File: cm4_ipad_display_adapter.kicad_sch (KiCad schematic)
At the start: 2 parts, among them J4 Conn_01x02_Female, U2 MIC5504-1.8YM5

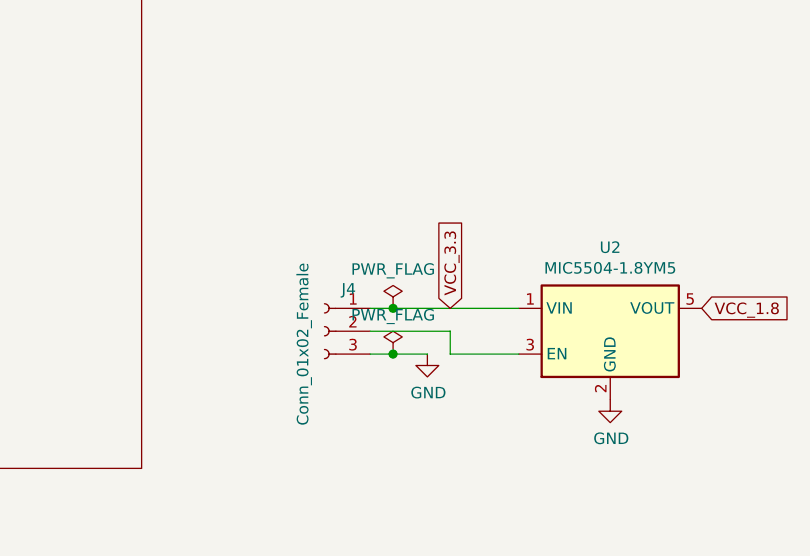
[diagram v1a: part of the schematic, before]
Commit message: Fix ERC errors
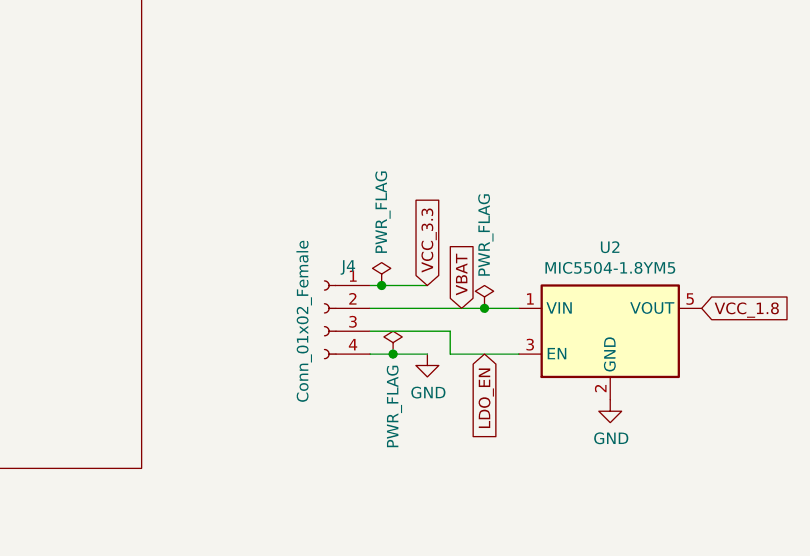
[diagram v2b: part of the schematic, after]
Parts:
- J4: symbol Connector:Conn_01x03_Female -> Connector:Conn_01x04_Female
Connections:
- net GND: now also J4.4 (Pin_4); no longer J4.3 (Pin_3)
- net VCC_3.3: no longer U2.1 (VIN)
- net LDO_EN: now reaches U2.3 (EN)
- net LDO_EN: now also J4.3 (Pin_3); no longer J4.2 (Pin_2)
- new net VBAT: J4.2 (Pin_2), U2.1 (VIN)

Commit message: Add footprints for LED driver HEAD associated components, route them. Fix DRC issues, and add an edge cut.
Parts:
- J4: footprint Connector_PinHeader_2.54mm:PinHeader_1x03_P2.54mm_Vertical -> Connector_PinHeader_2.54mm:PinHeader_1x04_P2.54mm_Vertical
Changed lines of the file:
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@@
     (property "Reference" "J4" (id 0) (at 128.422 85.503 0))
     (property "Value" "Conn_01x02_Female" (id 1) (at 123.3424 91.6113 90))
-    (property "Footprint" "Connector_PinHeader_2.54mm:PinHeader_1x03_P2.54mm_Vertical" (id 2) (at 125.73 90.17 0)
+    (property "Footprint" "Connector_PinHeader_2.54mm:PinHeader_1x04_P2.54mm_Vertical" (id 2) (at 125.73 90.17 0)
       (effects (font (size 1.27 1.27)) hide)
     )
@@
     )
     (path "/a946a672-0361-4eb9-a0a1-9c0b5f6de790"
-      (reference "J4") (unit 1) (value "Conn_01x02_Female") (footprint "Connector_PinHeader_2.54mm:PinHeader_1x03_P2.54mm_Vertical")
+      (reference "J4") (unit 1) (value "Conn_01x02_Female") (footprint "Connector_PinHeader_2.54mm:PinHeader_1x04_P2.54mm_Vertical")
     )
     (path "/7cf1659e-8585-4172-8c4c-c99ac927965b"

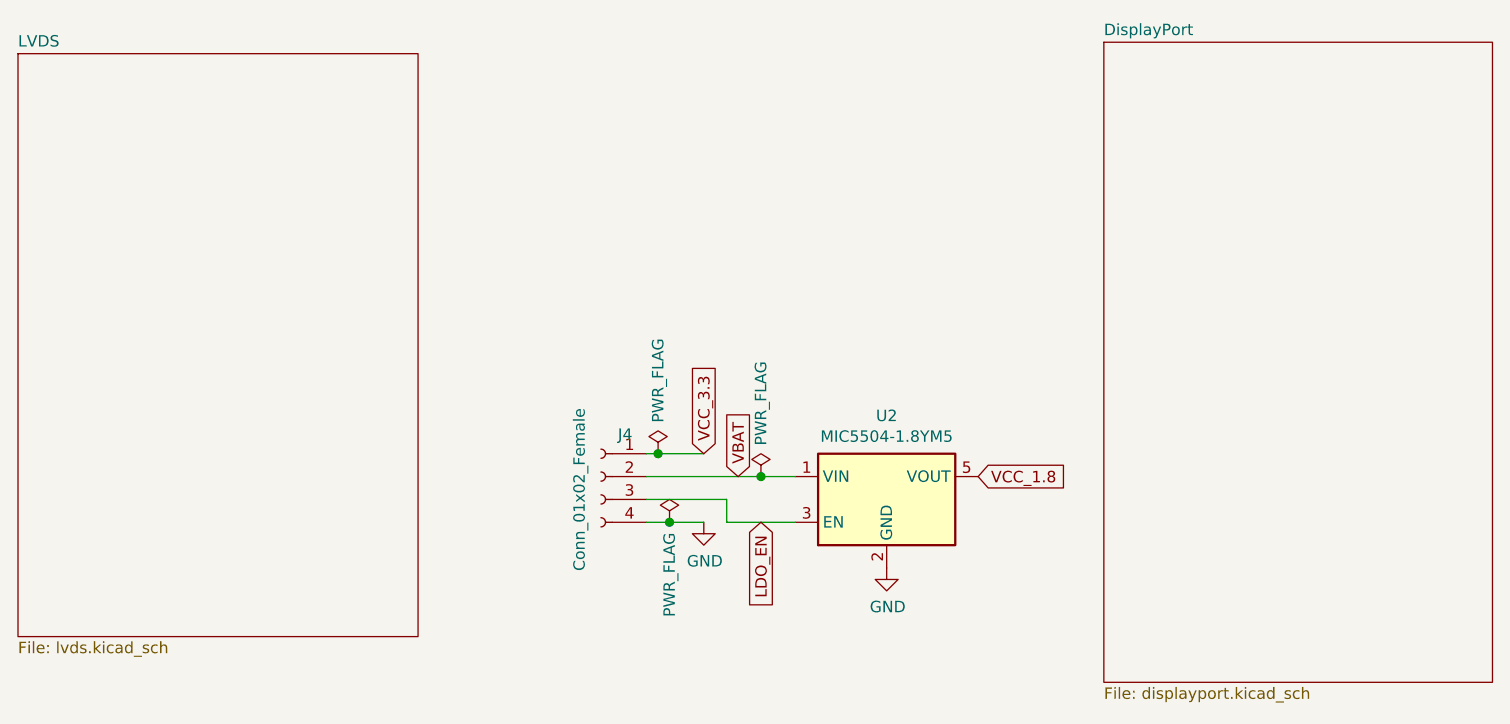
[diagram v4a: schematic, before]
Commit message: rearrange J4 pins to make traces for LDO simpler.
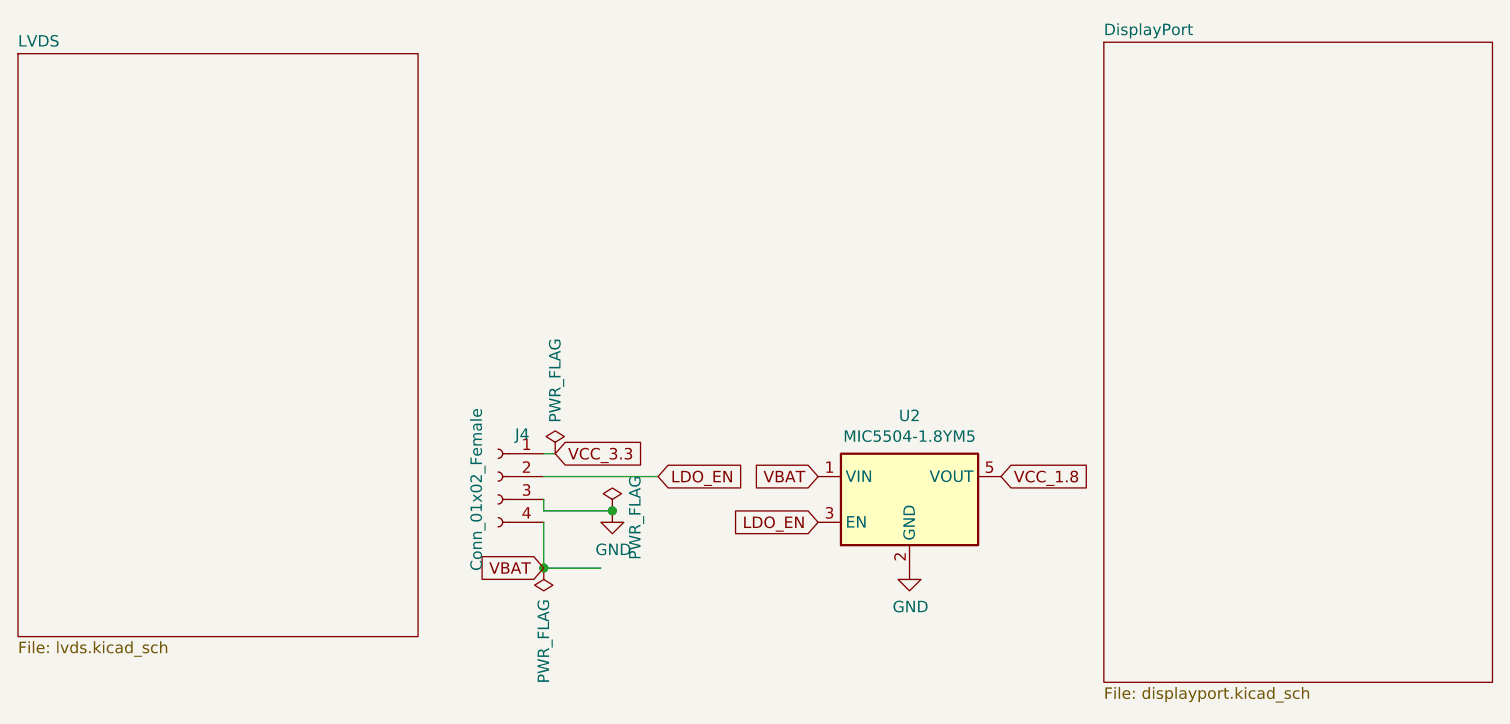
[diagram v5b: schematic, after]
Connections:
- net GND: now also J4.3 (Pin_3); no longer J4.4 (Pin_4)
- net LDO_EN: now also J4.2 (Pin_2); no longer J4.3 (Pin_3)
- net VBAT: now also J4.4 (Pin_4); no longer J4.2 (Pin_2)
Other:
- moved on the sheet: J4, U2
